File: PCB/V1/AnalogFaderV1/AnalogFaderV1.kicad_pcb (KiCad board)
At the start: 2 copper layers, 24.1 x 19.1 mm, 22 parts, among them J1 USB_B_Micro, SW1 SW_DIP_x03, U1 LMV324A

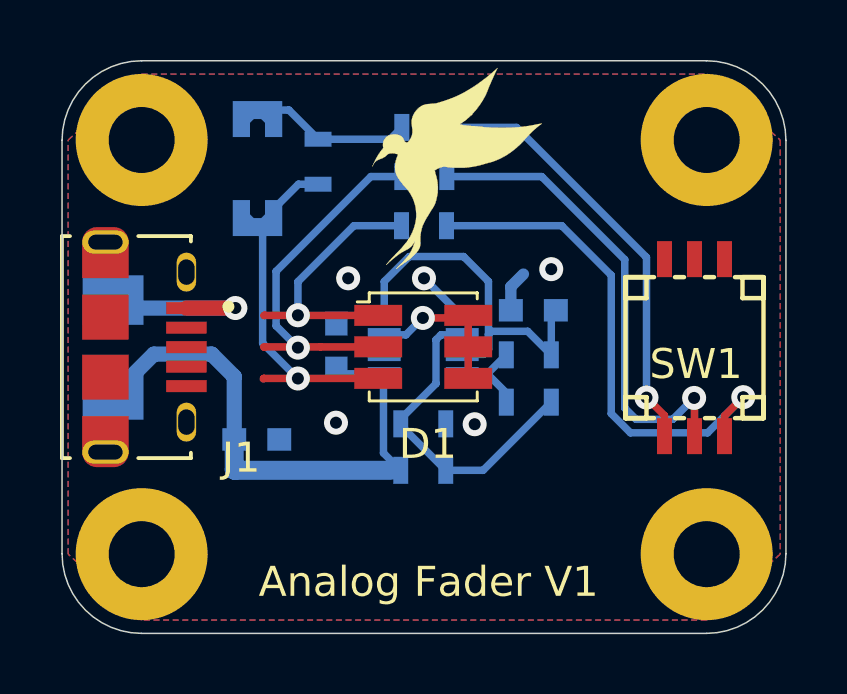
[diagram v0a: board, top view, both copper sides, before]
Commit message: Completed Kicad PCB for V1
Finish PCB for V1 of the analog fader circuit.
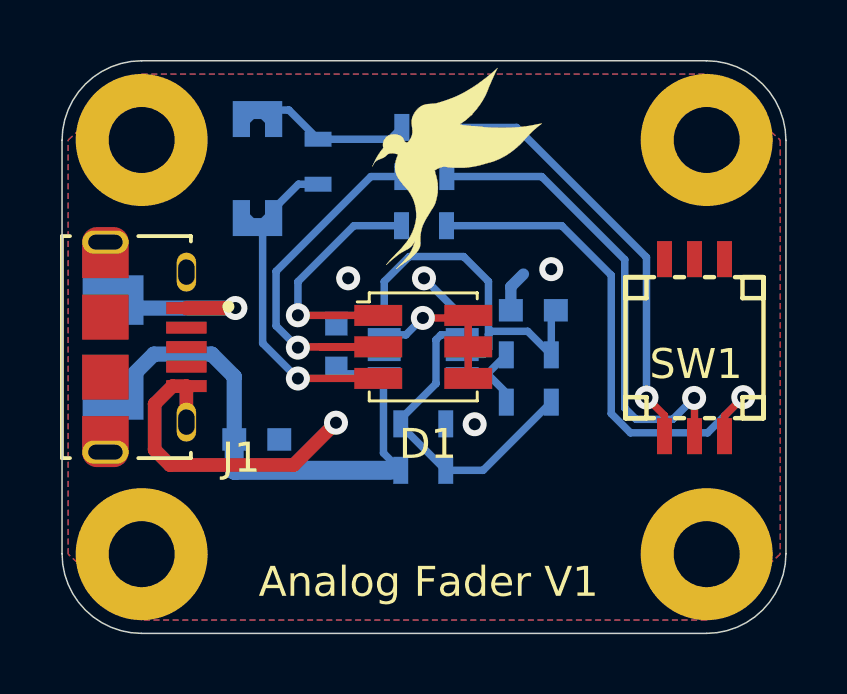
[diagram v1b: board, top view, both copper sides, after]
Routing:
- net GND: track 3.51 -> 14.4 mm
- net Net-(D1-Pad3): track 12.9 -> 11.8 mm
- net Net-(D1-Pad1): track 9.16 -> 8.03 mm
- net Net-(D1-Pad2): track 12.2 -> 13.0 mm
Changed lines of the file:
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@@
     (thickness 1.6)
     (drawings 19)
-    (tracks 123)
+    (tracks 129)
     (zones 0)
     (modules 22)
@@
     (visible_elements 7FFFFFFF)
     (pcbplotparams
-      (layerselection 0x010fc_ffffffff)
+      (layerselection 0x010f0_ffffffff)
       (usegerberextensions false)
-      (usegerberattributes true)
-      (usegerberadvancedattributes true)
-      (creategerberjobfile true)
+      (usegerberattributes false)
+      (usegerberadvancedattributes false)
+      (creategerberjobfile false)
       (excludeedgelayer true)
       (linewidth 0.100000)
@@
       (psa4output false)
       (plotreference true)
-      (plotvalue true)
+      (plotvalue false)
       (plotinvisibletext false)
-      (padsonsilk false)
+      (padsonsilk true)
       (subtractmaskfromsilk false)
       (outputformat 1)
       (mirror false)
-      (drillshape 1)
+      (drillshape 0)
       (scaleselection 1)
-      (outputdirectory ""))
+      (outputdirectory "gerber/"))
   )
   (net 0 "")
@@
       (effects (font (size 1 1) (thickness 0.15)) (justify mirror))
     )
-    (fp_text user %R (at 0 0 90) (layer B.Fab)
-      (effects (font (size 0.4 0.4) (thickness 0.075)) (justify mirror))
-    )
     (fp_line (start -0.8 -0.4) (end -0.8 0.4) (layer B.Fab) (width 0.1))
     (fp_line (start 0.8 -0.4) (end -0.8 -0.4) (layer B.Fab) (width 0.1))
@@
     (fp_line (start 1.25 -0.7) (end 1.25 0.7) (layer B.CrtYd) (width 0.05))
     (fp_line (start 1.25 -0.7) (end -1.25 -0.7) (layer B.CrtYd) (width 0.05))
+    (fp_text user %R (at 0 0 90) (layer B.Fab)
+      (effects (font (size 0.4 0.4) (thickness 0.075)) (justify mirror))
+    )
     (pad 1 smd rect (at -0.75 0 270) (size 0.5 0.9) (layers B.Cu B.Paste B.Mask)
       (net 15 "Net-(D2-Pad1)"))
@@
       (effects (font (size 1 1) (thickness 0.15)))
     )
-    (fp_text user %R (at 0.3 0) (layer F.Fab)
-      (effects (font (size 1 1) (thickness 0.15)))
-    )
     (fp_circle (center 0 0) (end 2.2 0) (layer Cmts.User) (width 0.15))
     (fp_circle (center 0 0) (end 2.45 0) (layer F.CrtYd) (width 0.05))
+    (fp_text user %R (at 0.3 0) (layer F.Fab)
+      (effects (font (size 1 1) (thickness 0.15)))
+    )
     (pad 1 thru_hole circle (at 0 0) (size 4.399999 4.399999) (drill 2.2) (layers *.Cu *.Mask)
       (net 2 GND) (zone_connect 2))
@@
       (effects (font (size 1 1) (thickness 0.15)))
     )
-    (fp_text user %R (at 0.3 0) (layer F.Fab)
-      (effects (font (size 1 1) (thickness 0.15)))
-    )
     (fp_circle (center 0 0) (end 2.2 0) (layer Cmts.User) (width 0.15))
     (fp_circle (center 0 0) (end 2.45 0) (layer F.CrtYd) (width 0.05))
+    (fp_text user %R (at 0.3 0) (layer F.Fab)
+      (effects (font (size 1 1) (thickness 0.15)))
+    )
     (pad 1 thru_hole circle (at 0 0) (size 4.399999 4.399999) (drill 2.2) (layers *.Cu *.Mask)
       (net 2 GND) (zone_connect 2))
@@
   (via (at 124.0155 51.4604) (size 0.8) (drill 0.4) (layers F.Cu B.Cu) (net 2))
   (via (at 126.5682 46.2915) (size 0.8) (drill 0.4) (layers F.Cu B.Cu) (net 2))
+  (segment (start 114.4069 50.1899) (end 114.4069 51.3899) (width 0.4572) (layer F.Cu) (net 2))
+  (segment (start 114.4069 50.1899) (end 113.9449 50.1899) (width 0.4572) (layer F.Cu) (net 2))
+  (segment (start 113.9449 50.1899) (end 113.3475 50.7873) (width 0.4572) (layer F.Cu) (net 2))
+  (segment (start 113.3475 50.7873) (end 113.3475 52.3113) (width 0.4572) (layer F.Cu) (net 2))
+  (segment (start 113.3475 52.3113) (end 113.8555 52.8193) (width 0.4572) (layer F.Cu) (net 2))
+  (segment (start 117.983 52.8193) (end 119.3927 51.4096) (width 0.4572) (layer F.Cu) (net 2))
+  (segment (start 113.8555 52.8193) (end 117.983 52.8193) (width 0.4572) (layer F.Cu) (net 2))
   (segment (start 120.975999 49.806101) (end 121.001 49.7811) (width 0.25) (layer B.Cu) (net 3))
   (segment (start 120.975999 52.422099) (end 120.975999 49.806101) (width 0.25) (layer B.Cu) (net 3))
@@
   (segment (start 111.9632 50.4825) (end 113.3221 49.1236) (width 0.508) (layer B.Cu) (net 3))
   (via (at 118.1227 47.8282) (size 0.8) (drill 0.4) (layers F.Cu B.Cu) (net 4))
-  (segment (start 117.0219 47.8323) (end 117.0178 47.8282) (width 0.25) (layer F.Cu) (net 4))
-  (segment (start 117.001 47.8323) (end 116.9924 47.8409) (width 0.25) (layer F.Cu) (net 4))
-  (segment (start 120.801 47.8323) (end 117.001 47.8323) (width 0.25) (layer F.Cu) (net 4))
   (segment (start 119.9896 44.8437) (end 121.5771 44.8437) (width 0.25) (layer B.Cu) (net 4))
   (segment (start 118.1227 46.7106) (end 119.9896 44.8437) (width 0.25) (layer B.Cu) (net 4))
   (segment (start 118.1227 47.8282) (end 118.1227 46.7106) (width 0.25) (layer B.Cu) (net 4))
+  (segment (start 118.1268 47.8323) (end 118.1227 47.8282) (width 0.25) (layer F.Cu) (net 4))
+  (segment (start 120.801 47.8323) (end 118.1268 47.8323) (width 0.25) (layer F.Cu) (net 4))
   (via (at 118.1227 48.9077) (size 0.8) (drill 0.4) (layers F.Cu B.Cu) (net 5))
-  (segment (start 117.0178 48.8823) (end 117.0051 48.895) (width 0.25) (layer F.Cu) (net 5))
-  (segment (start 118.872 48.8823) (end 116.9797 48.8823) (width 0.25) (layer F.Cu) (net 5))
   (segment (start 118.872 48.8823) (end 120.801 48.8823) (width 0.25) (layer F.Cu) (net 5))
   (segment (start 120.554898 43.2054) (end 121.5884 43.2054) (width 0.25) (layer B.Cu) (net 5))
@@
   (segment (start 117.397699 48.182699) (end 117.397699 46.362599) (width 0.25) (layer B.Cu) (net 5))
   (segment (start 118.1227 48.9077) (end 117.397699 48.182699) (width 0.25) (layer B.Cu) (net 5))
+  (segment (start 118.1481 48.8823) (end 118.1227 48.9077) (width 0.25) (layer F.Cu) (net 5))
+  (segment (start 120.801 48.8823) (end 118.1481 48.8823) (width 0.25) (layer F.Cu) (net 5))
   (segment (start 121.001 49.1311) (end 121.001 48.4811) (width 0.25) (layer B.Cu) (net 6))
   (segment (start 123.801 47.8323) (end 123.801 48.8823) (width 0.25) (layer F.Cu) (net 6))
@@
   (segment (start 122.2883 47.9171) (end 123.7162 47.9171) (width 0.25) (layer F.Cu) (net 6))
   (via (at 116.0399 47.5869) (size 0.8) (drill 0.4) (layers F.Cu B.Cu) (net 7))
-  (segment (start 116.0369 47.5899) (end 116.0399 47.5869) (width 0.25) (layer F.Cu) (net 7))
-  (segment (start 114.4069 47.5899) (end 116.0369 47.5899) (width 0.508) (layer F.Cu) (net 7))
   (segment (start 112.2276 47.5869) (end 111.9632 47.3225) (width 0.25) (layer B.Cu) (net 7))
   (segment (start 116.0399 47.5869) (end 112.2276 47.5869) (width 0.508) (layer B.Cu) (net 7))
+  (segment (start 116.0369 47.5899) (end 116.0399 47.5869) (width 0.25) (layer F.Cu) (net 7))
+  (segment (start 114.4069 47.5899) (end 116.0369 47.5899) (width 0.4826) (layer F.Cu) (net 7))
   (segment (start 124.2963 52.9971) (end 123.051 52.9971) (width 0.25) (layer B.Cu) (net 11))
   (segment (start 126.5696 50.7238) (end 124.2963 52.9971) (width 0.25) (layer B.Cu) (net 11))
@@
   (segment (start 125.4125 41.5671) (end 129.7432 45.8978) (width 0.25) (layer B.Cu) (net 16))
   (via (at 118.1227 49.9364) (size 0.8) (drill 0.4) (layers F.Cu B.Cu) (net 17))
-  (segment (start 116.9838 49.9323) (end 116.967 49.9491) (width 0.25) (layer F.Cu) (net 17))
-  (segment (start 120.801 49.9323) (end 116.9838 49.9323) (width 0.25) (layer F.Cu) (net 17))
   (segment (start 117.314 44.3512) (end 116.7765 44.8887) (width 0.25) (layer B.Cu) (net 17))
   (segment (start 117.314 44.2887) (end 117.314 44.3512) (width 0.25) (layer B.Cu) (net 17))
@@
   (segment (start 116.947689 48.761389) (end 116.947689 45.059889) (width 0.25) (layer B.Cu) (net 17))
   (segment (start 118.1227 49.9364) (end 116.947689 48.761389) (width 0.25) (layer B.Cu) (net 17))
+  (segment (start 118.1268 49.9323) (end 118.1227 49.9364) (width 0.25) (layer F.Cu) (net 17))
+  (segment (start 120.801 49.9323) (end 118.1268 49.9323) (width 0.25) (layer F.Cu) (net 17))
   (zone (net 2) (net_name GND) (layer B.Cu) (hatch edge 0.508)
     (connect_pads (clearance 0.508))
